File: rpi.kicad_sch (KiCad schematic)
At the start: 75 parts, among them J1 Conn_02x08_Counter_Clockwise_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, J101 Conn_01x03_Pin, J4 Conn_01x04_Pin, J5 Conn_02x08_Counter_Clockwise_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, J6 2169890001, J7 430450800, U3 RASPBERRY_PI_ZERO_2_W

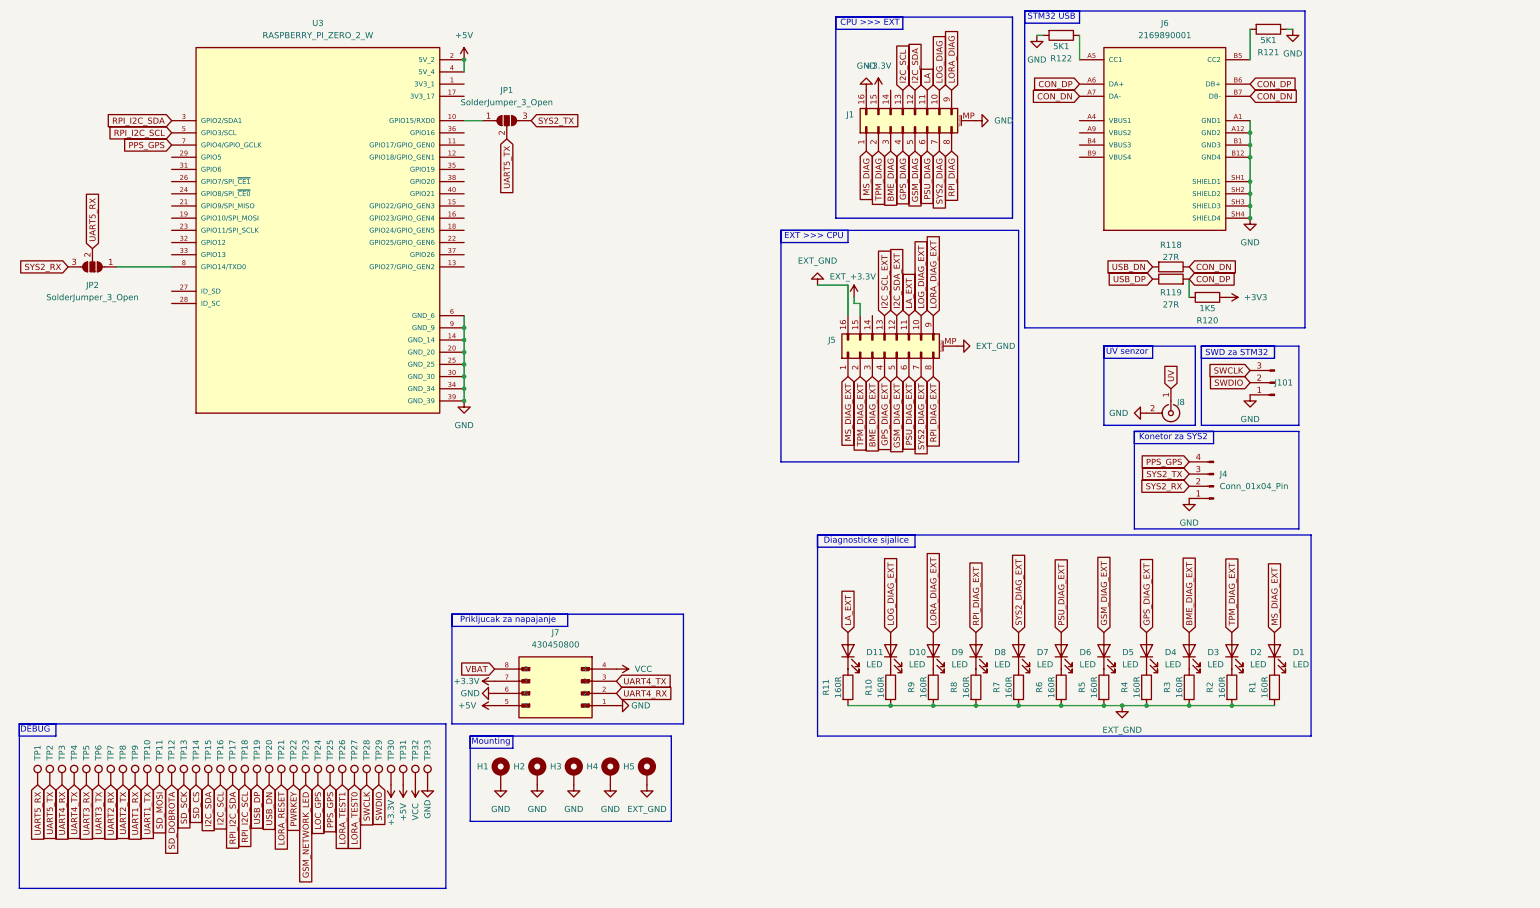
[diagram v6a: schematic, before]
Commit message: Znacajne izmene seme i pcb-a
Napravljen nov layout
dodat konektor za gpio
dodat konektor za eksterna merenja vetra
izmenjene diag lampice
izmenjen konektor za ext plocu
razno
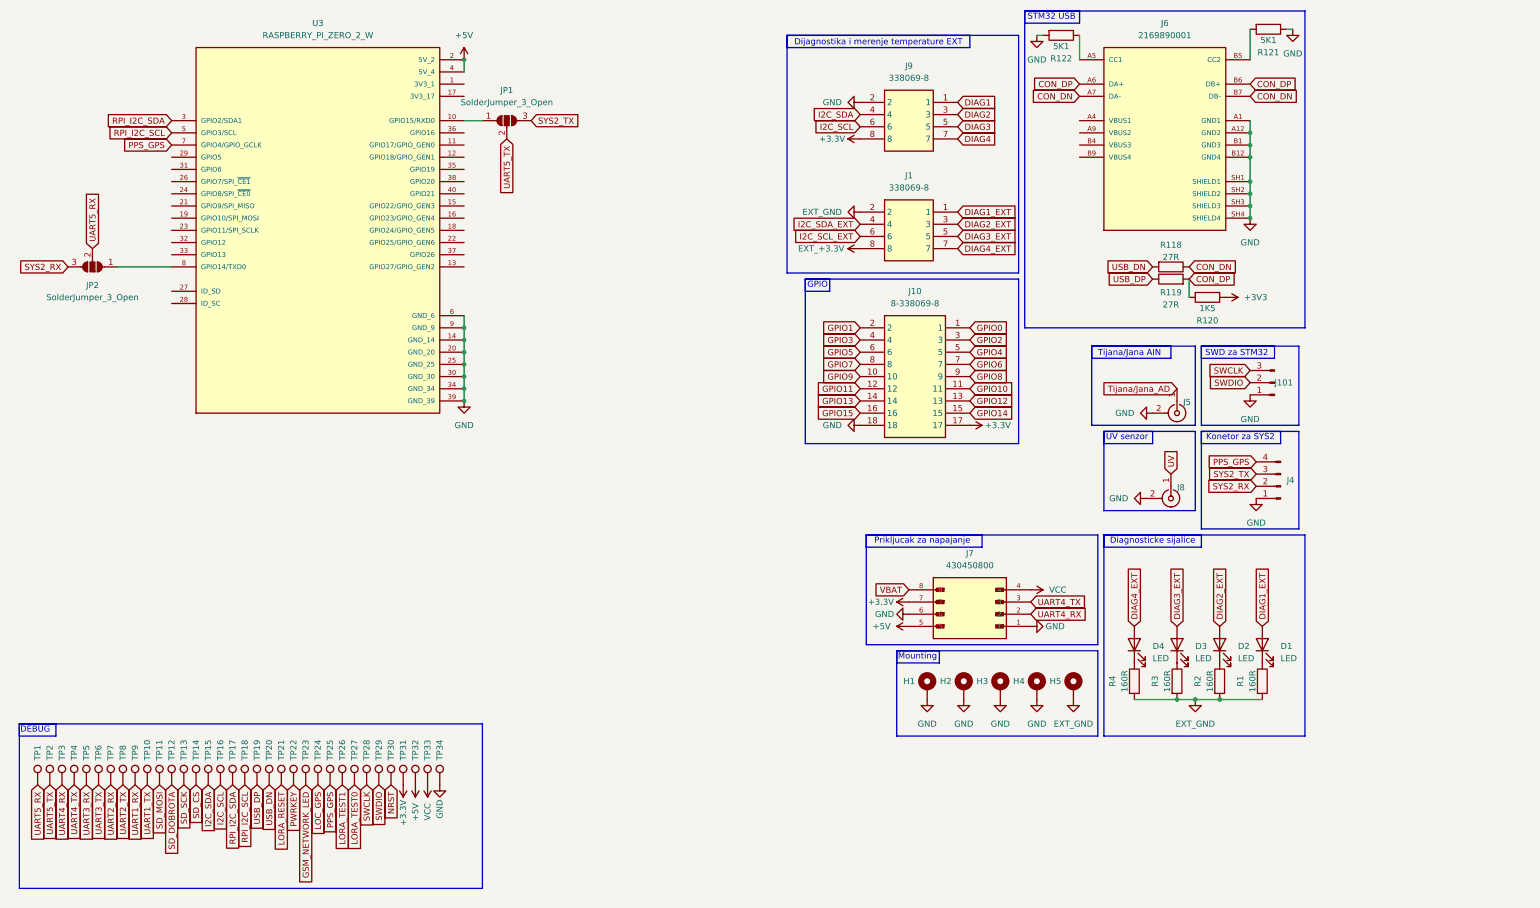
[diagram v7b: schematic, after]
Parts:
- removed D10, D11, D5, D6, D7, D8, D9: LED, LED_SMD:LED_1206_3216Metric_Pad1.42x1.75mm_HandSolder, symbol Device:LED
- removed J1, J5: Conn_02x08_Counter_Clockwise_MountingPin, Connector_FFC-FPC:Hirose_FH12-16S-0.5SH_1x16-1MP_P0.50mm_Horizontal, symbol Connector_Generic_MountingPin:Conn_02x08_Counter_Clockwise_MountingPin
- removed R10, R11, R5, R6, R7, R8, R9: 160R, Resistor_SMD:R_1206_3216Metric_Pad1.30x1.75mm_HandSolder, symbol Device:R
- added J1, J9: 338069-8, 3380698, symbol 338069-8:338069-8
- added J10: 8-338069-8, 83380698, symbol 8-338069-8:8-338069-8
- added J5: ~, Connector_Coaxial:SMA_Amphenol_132134-16_Vertical, symbol Connector:Conn_Coaxial
- added TP34: TestPoint, TestPoint:TestPoint_Pad_D1.0mm, symbol Connector:TestPoint
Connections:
- net +3.3V: now also TP31.1, J10.17, J9.8; no longer TP30.1
- net +5V: now also TP32.1; no longer TP31.1
- net EXT_+3.3V: now also J1.8
- net EXT_GND: now also J1.2
- net GND: now also J10.18, J5.2 (Ext), J9.2, TP34.1; no longer TP33.1
- net I2C_SCL: now also J9.6
- net I2C_SCL_EXT: now also J1.6
- net I2C_SDA: now also J9.4
- net I2C_SDA_EXT: now also J1.4
- net VCC: now also TP33.1; no longer TP32.1
- net BME_DIAG_EXT renamed DIAG3_EXT
- net DIAG3_EXT: now also J1.5
- net GPS_DIAG_EXT renamed DIAG4_EXT
- net DIAG4_EXT: now also J1.7
- net MS_DIAG_EXT renamed DIAG1_EXT
- net DIAG1_EXT: now also J1.1
- net TPM_DIAG_EXT renamed DIAG2_EXT
- net DIAG2_EXT: now also J1.3
- new net DIAG1: J9.1
- new net DIAG2: J9.3
- new net DIAG3: J9.5
- new net DIAG4: J9.7
- new net GPIO0: J10.1
- new net GPIO1: J10.2
- new net GPIO10: J10.11
- new net GPIO11: J10.12
- new net GPIO12: J10.13
- new net GPIO13: J10.14
- new net GPIO14: J10.15
- new net GPIO15: J10.16
- new net GPIO2: J10.3
- new net GPIO3: J10.4
- new net GPIO4: J10.5
- new net GPIO5: J10.6
- new net GPIO6: J10.7
- new net GPIO7: J10.8
- new net GPIO8: J10.9
- new net GPIO9: J10.10
- new net NRST: TP30.1
- new net Tijana/Jana_AD: J5.1 (In)
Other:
- note added: "Dijagnostika i merenje temperature EXT"
- note added: "GPIO"
- note added: "Tijana/Jana AIN"
- note removed: "CPU >>> EXT"
- note removed: "EXT >>> CPU"
- moved on the sheet: D1, D2, D3, D4, H1, H2, H3, H4, H5, J4, J7, J8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
